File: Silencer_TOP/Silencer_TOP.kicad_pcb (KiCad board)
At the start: 2 copper layers, 36 parts, among them T100 2N3904, T101 2N3904, T102 2N3904, T103 2N3904

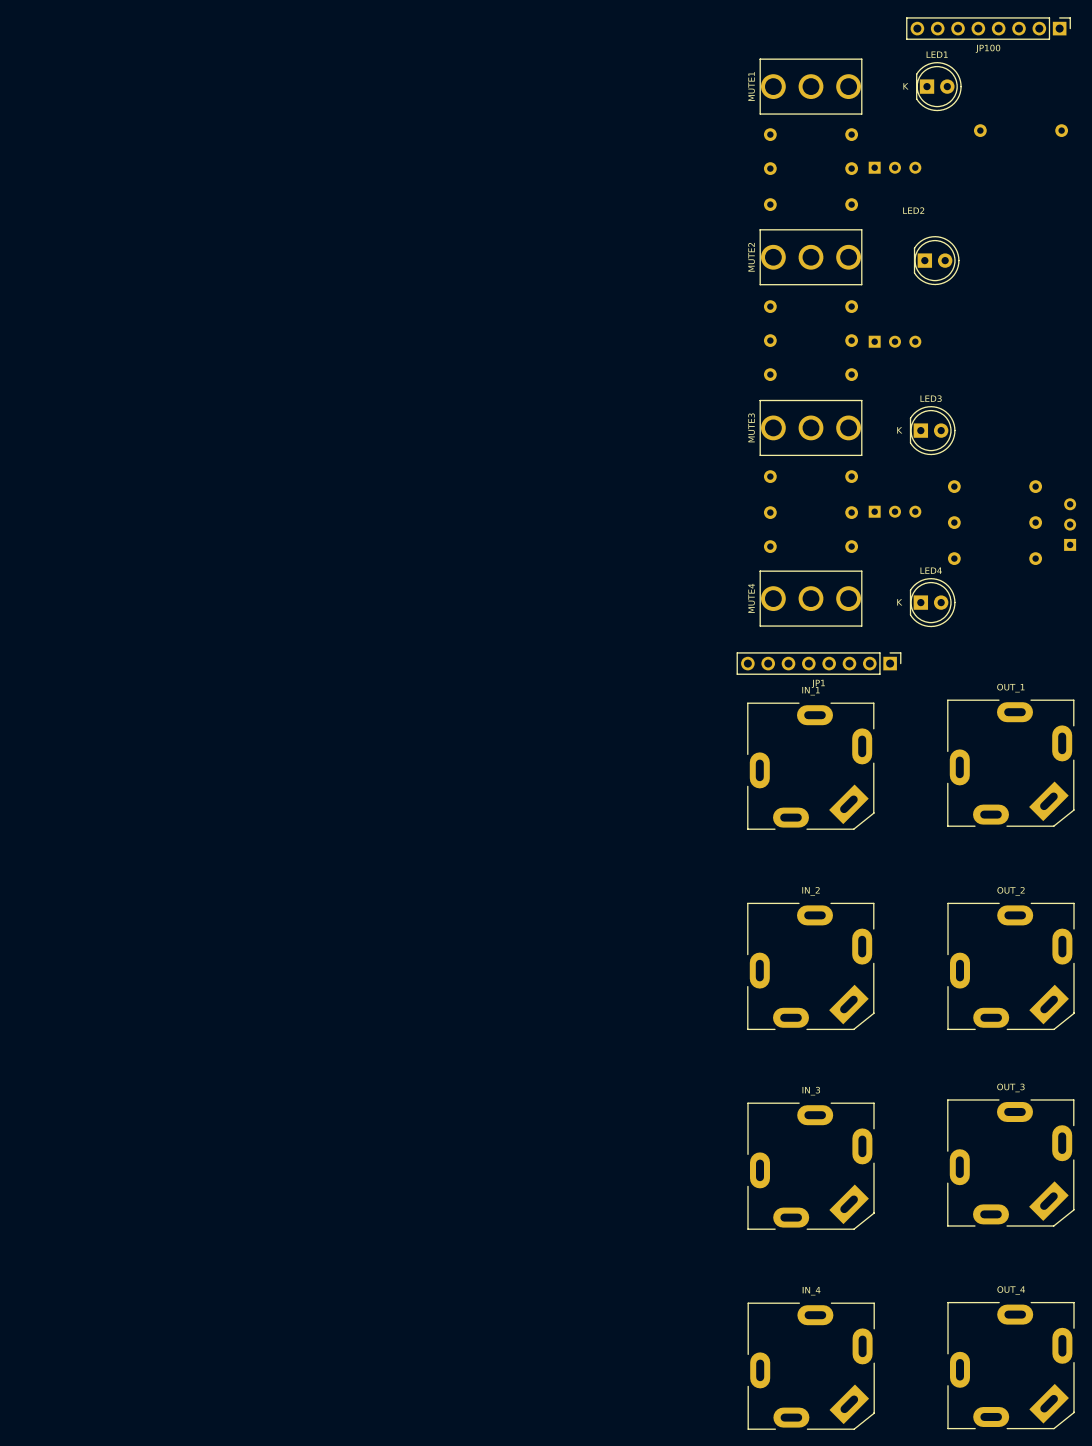
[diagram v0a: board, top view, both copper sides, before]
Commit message: Refactor Top and Bottom Schematics.
Had to move input/output jacks to bottom board.  This required a full refactoring of both and will mean re-doing the pcb layout of the top board.
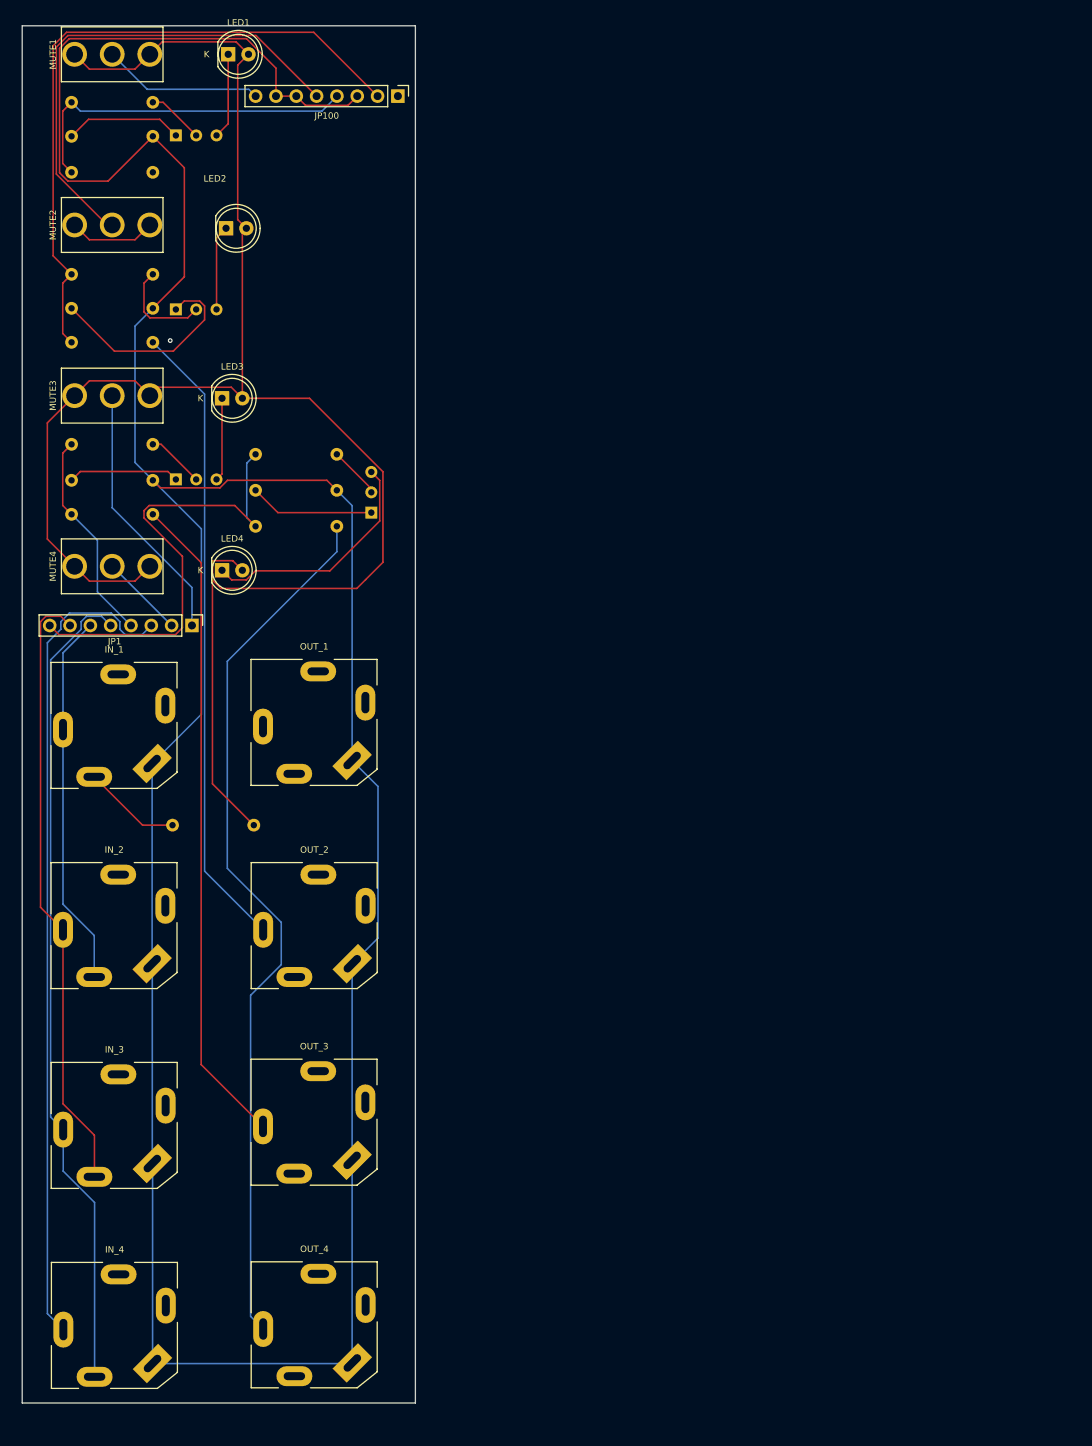
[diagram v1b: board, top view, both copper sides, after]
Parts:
- moved R111 133.2 mm to (29.9, 112.4)
- moved T103 87.4 mm to (44.6, 73.4)
- moved LED1 87.4 mm to (26.8, 16.1)
- moved LED2 87.4 mm to (26.5, 37.8)
- moved LED3 87.4 mm to (26.0, 59.1)
- moved LED4 87.4 mm to (26.0, 80.6)
- moved MUTE1 87.4 mm to (12.2, 16.1)
- moved MUTE2 87.4 mm to (12.2, 37.4)
- moved MUTE3 87.4 mm to (12.2, 58.7)
- moved MUTE4 87.4 mm to (12.2, 80.1)
- moved R100 87.4 mm to (7.17, 22.1)
- moved R101 87.4 mm to (7.17, 30.8)
- moved R102 87.4 mm to (7.17, 26.3)
- moved R103 87.4 mm to (7.17, 43.6)
- moved R104 87.4 mm to (7.17, 52.1)
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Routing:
- net GND_1: track 0.00 -> 399.1 mm
- net +12V_1: track 0.00 -> 236.0 mm
- net Net-(OUT_4-PadT): track 0.00 -> 111.0 mm
- net IN4_T: track 0.00 -> 103.9 mm
- net IN3_T: track 0.00 -> 102.7 mm
- net LED2_T: track 0.00 -> 83.5 mm
- net Net-(OUT_3-PadT): track 0.00 -> 82.2 mm
- net Net-(OUT_2-PadT): track 0.00 -> 79.2 mm
- net IN2_T: track 0.00 -> 76.6 mm
- net M2_T: track 0.00 -> 61.8 mm
- net LED4_T: track 0.00 -> 59.2 mm
- net IN1_T: track 0.00 -> 47.0 mm
- net LED1_T: track 0.00 -> 44.1 mm
- net M3_T: track 0.00 -> 32.9 mm
- net Net-(LED4-K): track 0.00 -> 29.8 mm
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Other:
- board outline added: 49.1 x 172.2 mm

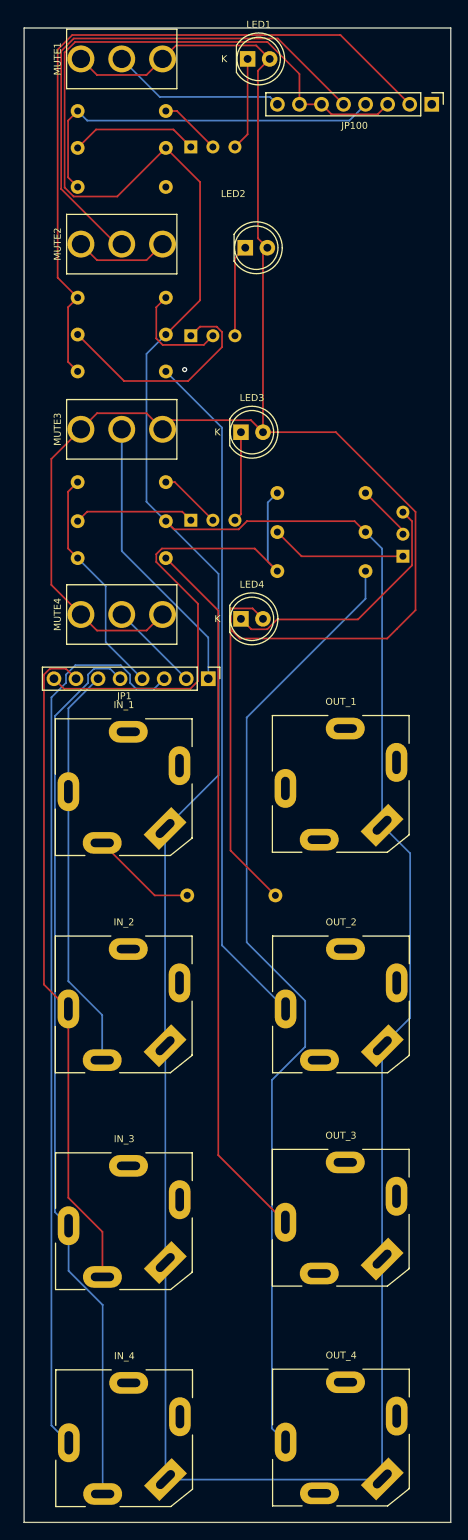
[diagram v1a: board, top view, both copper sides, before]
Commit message: Top Board Layout lined up and routed.
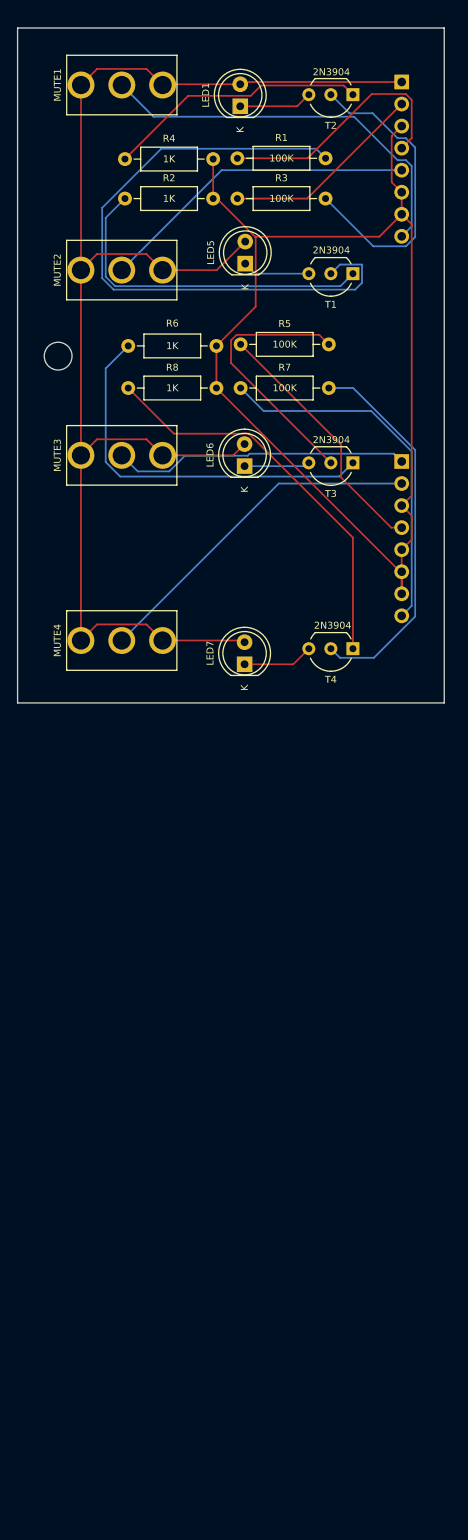
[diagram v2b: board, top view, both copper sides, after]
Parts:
- removed GRAF3: CC0 logo, AO_tht:CC0_logo
- removed IN_1, IN_2, IN_3, IN_4, OUT_1, OUT_2, OUT_3, OUT_4: AudioJack2_SwitchT, AO_tht:Jack_6.35mm_PJ_629HAN_slots
- removed LED2, LED3, LED4: LED_red, AO_tht:LED_D5.0mm
- removed R100, R103, R107, R109: 100K, AO_tht:R_Axial_DIN0207_L6.3mm_D2.5mm_P10.16mm_Horizontal
- removed R101, R102, R104, R105, R106, R108, R110, R112: 1K, AO_tht:R_Axial_DIN0207_L6.3mm_D2.5mm_P10.16mm_Horizontal
- removed R111: 4K7, AO_tht:R_Axial_DIN0207_L6.3mm_D2.5mm_P10.16mm_Horizontal
- removed T100, T101, T102, T103: 2N3904, AO_tht:TO-92_Inline_Wide
- added LED5: LED_red, AO_tht:LED_D5.0mm, F.Cu at (26.5, 39.6)
- added LED6: LED_red, AO_tht:LED_D5.0mm, F.Cu at (26.4, 63.0)
- added LED7: LED_red, AO_tht:LED_D5.0mm, F.Cu at (26.4, 85.8)
- added R1: 100K, AO_tht:R_Axial_DIN0207_L6.3mm_D2.5mm_P10.16mm_Horizontal, F.Cu at (25.6, 27.5)
- added R2: 1K, AO_tht:R_Axial_DIN0207_L6.3mm_D2.5mm_P10.16mm_Horizontal, F.Cu at (12.6, 32.1)
- added R3: 100K, AO_tht:R_Axial_DIN0207_L6.3mm_D2.5mm_P10.16mm_Horizontal, F.Cu at (25.6, 32.1)
- added R4: 1K, AO_tht:R_Axial_DIN0207_L6.3mm_D2.5mm_P10.16mm_Horizontal, F.Cu at (12.6, 27.6)
- added R5: 100K, AO_tht:R_Axial_DIN0207_L6.3mm_D2.5mm_P10.16mm_Horizontal, F.Cu at (25.9, 48.9)
- added R6: 1K, AO_tht:R_Axial_DIN0207_L6.3mm_D2.5mm_P10.16mm_Horizontal, F.Cu at (13.0, 49.1)
- added R7: 100K, AO_tht:R_Axial_DIN0207_L6.3mm_D2.5mm_P10.16mm_Horizontal, F.Cu at (25.9, 54.0)
- added R8: 1K, AO_tht:R_Axial_DIN0207_L6.3mm_D2.5mm_P10.16mm_Horizontal, F.Cu at (13.0, 54.0)
- added REF**: MountingHole_3.2mm_M3, AO_tht:MountingHole_3.2mm_M3, F.Cu at (4.92, 50.3)
- added T1: 2N3904, AO_tht:TO-92_Inline_Wide, F.Cu at (38.9, 40.8)
- added T2: 2N3904, AO_tht:TO-92_Inline_Wide, F.Cu at (38.9, 20.2)
- added T3: 2N3904, AO_tht:TO-92_Inline_Wide, F.Cu at (38.9, 62.6)
- added T4: 2N3904, AO_tht:TO-92_Inline_Wide, F.Cu at (38.9, 84.0)
- JP1, JP100: moved to B.Cu
- moved JP1 35.0 mm to (44.4, 71.3), turned to -90 degrees
- moved JP100 8.15 mm to (44.4, 27.6), turned to -90 degrees
- moved LED1 5.52 mm to (25.9, 21.5), turned to 90 degrees
- moved MUTE1 3.01 mm to (12.3, 19.1)
- moved MUTE3 3.00 mm to (12.2, 61.7)
- moved MUTE4 3.00 mm to (12.2, 83.1)
- moved MUTE2 2.99 mm to (12.2, 40.4)
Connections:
- JP1 pad 3: IN4_T -> GND_1
- JP1 pad 5: IN3_T -> GND_1
- JP1 pad 6: IN1_T -> GND_1
- JP1 pad 7: IN2_T -> GND_1
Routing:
- net GND_1: track 399.1 -> 137.8 mm
- net Net-(OUT_4-PadT): track 111.0 -> 0.00 mm
- net IN4_T: track 103.9 -> 0.00 mm
- net IN3_T: track 102.7 -> 0.00 mm
- net Net-(OUT_3-PadT): track 82.2 -> 0.00 mm
- net Net-(OUT_2-PadT): track 79.2 -> 0.00 mm
- net IN2_T: track 76.6 -> 0.00 mm
- net Net-(T1-B): track 0.00 -> 74.1 mm
- net +12V_1: track 236.0 -> 165.8 mm
- net LED2_T: track 83.5 -> 23.4 mm
- net IN1_T: track 47.0 -> 0.00 mm
- net Net-(T4-E): track 0.00 -> 45.8 mm
- net Net-(T3-E): track 0.00 -> 44.3 mm
- net Net-(T4-B): track 0.00 -> 44.2 mm
- net Net-(T1-E): track 0.00 -> 39.5 mm
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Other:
- board size 49.1 x 172.2 mm -> 49.1 x 77.8 mm

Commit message: Bottom board layout roughed out.  Routing began
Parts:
- renumbered JP100 to JP2
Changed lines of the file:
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@@
 		(descr "Through hole straight pin header, 1x08, 2.54mm pitch, single row")
 		(tags "Through hole pin header THT 1x08 2.54mm single row")
-		(property "Reference" "JP100"
+		(property "Reference" "JP2"
 			(at 0 2.33 90)
 			(layer "B.SilkS")
